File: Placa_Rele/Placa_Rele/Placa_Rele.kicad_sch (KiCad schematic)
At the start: 42 parts, among them J1 Screw_Terminal_Crusher1, J2 MixerScrewTerminal1, J3 FanScrewTerminal1, K1 FINDER-36.11, K2 FINDER-36.11, K3 FINDER-36.11, Q1 2N3904, Q2 2N3904, Q3 2N3904, U1 LM7805_TO220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

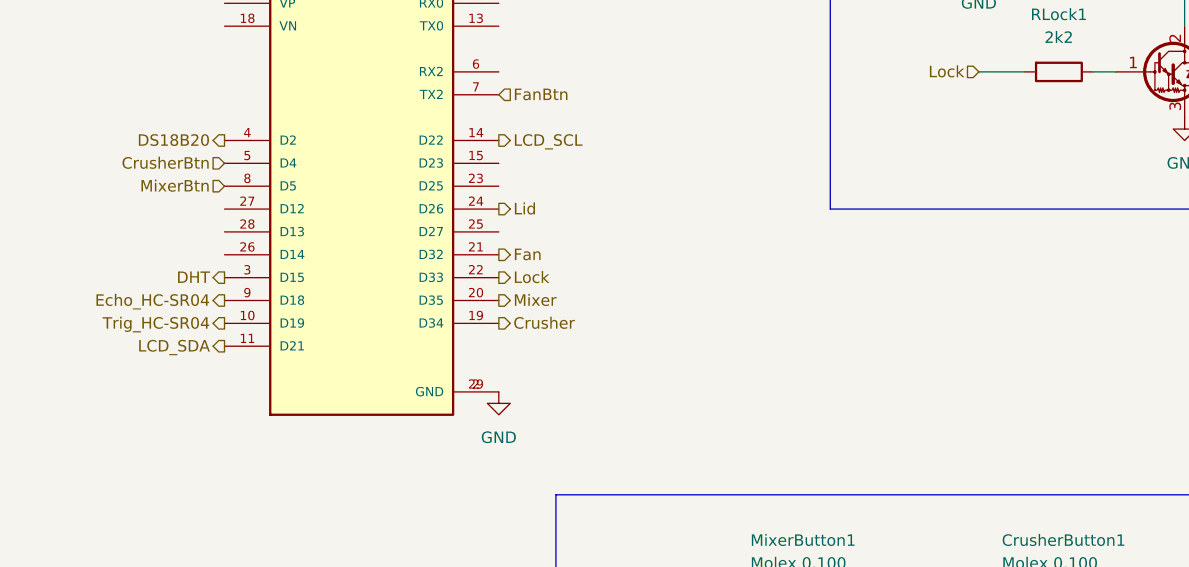
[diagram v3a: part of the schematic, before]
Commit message: feat: Agregado de placa para pcbway
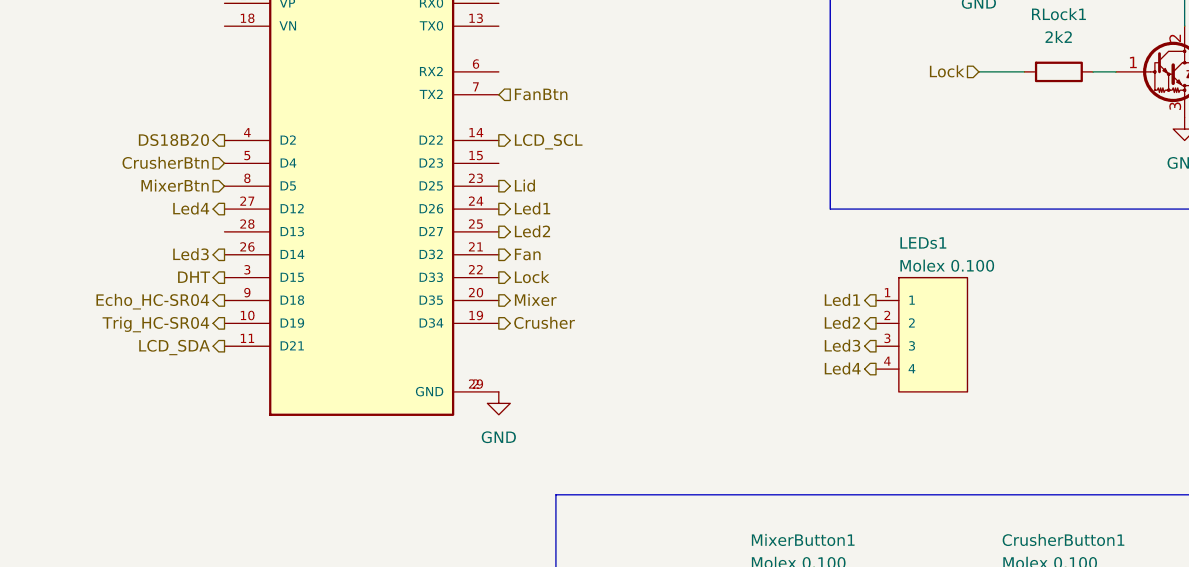
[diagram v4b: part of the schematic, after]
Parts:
- added LEDs1: Molex 0.100, Conectores_Molex:Molex_100_4pines, symbol Conectores_Molex:Molex_100_4pines
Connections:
- net Lid: now also U2.23 (D25); no longer U2.24 (D26)
- net Led2: now reaches U2.25 (D27)
- net Led2: now also LEDs1.2
- net Led3: now reaches U2.26 (D14)
- net Led3: now also LEDs1.3
- net Led4: now reaches U2.27 (D12)
- net Led4: now also LEDs1.4
- new net Led1: LEDs1.1, U2.24 (D26)
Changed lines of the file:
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@@
     (effects (font (size 1.27 1.27)) (justify left))
+  )
+  (hierarchical_label "Led1" (shape output) (at 232.41 106.68 180) (fields_autoplaced)
+    (effects (font (size 1.27 1.27)) (justify right))
   )
   (hierarchical_label "Mixer" (shape input) (at 119.38 109.22 0) (fields_autoplaced)
@@
     (effects (font (size 1.27 1.27)) (justify right))
   )
-  (hierarchical_label "Lid" (shape output) (at 190.5 96.52 0) (fields_autoplaced)
+  (hierarchical_label "Led1" (shape output) (at 190.5 96.52 0) (fields_autoplaced)
     (effects (font (size 1.27 1.27)) (justify left))
+  )
+  (hierarchical_label "Lid" (shape output) (at 190.5 93.98 0) (fields_autoplaced)
+    (effects (font (size 1.27 1.27)) (justify left))
+  )
+  (hierarchical_label "Led4" (shape output) (at 232.41 114.3 180) (fields_autoplaced)
+    (effects (font (size 1.27 1.27)) (justify right))
   )
   (hierarchical_label "Fan" (shape input) (at 119.38 152.4 0) (fields_autoplaced)
     (effects (font (size 1.27 1.27)) (justify left))
   )
+  (hierarchical_label "Led4" (shape output) (at 160.02 96.52 180) (fields_autoplaced)
+    (effects (font (size 1.27 1.27)) (justify right))
+  )
   (hierarchical_label "DHT" (shape input) (at 162.56 35.56 180) (fields_autoplaced)
     (effects (font (size 1.27 1.27)) (justify right))
@@
     (effects (font (size 1.27 1.27)) (justify right))
   )
+  (hierarchical_label "Led3" (shape output) (at 160.02 101.6 180) (fields_autoplaced)
+    (effects (font (size 1.27 1.27)) (justify right))
+  )
   (hierarchical_label "MixerBtn" (shape output) (at 208.28 144.78 180) (fields_autoplaced)
     (effects (font (size 1.27 1.27)) (justify right))
@@
     (effects (font (size 1.27 1.27)) (justify left))
   )
+  (hierarchical_label "Led3" (shape output) (at 232.41 111.76 180) (fields_autoplaced)
+    (effects (font (size 1.27 1.27)) (justify right))
+  )
   (hierarchical_label "Fan" (shape output) (at 190.5 101.6 0) (fields_autoplaced)
     (effects (font (size 1.27 1.27)) (justify left))
@@
     (effects (font (size 1.27 1.27)) (justify right))
   )
+  (hierarchical_label "Led2" (shape output) (at 232.41 109.22 180) (fields_autoplaced)
+    (effects (font (size 1.27 1.27)) (justify right))
+  )
   (hierarchical_label "3V3" (shape output) (at 190.5 66.04 0) (fields_autoplaced)
+    (effects (font (size 1.27 1.27)) (justify left))
+  )
+  (hierarchical_label "Led2" (shape output) (at 190.5 99.06 0) (fields_autoplaced)
     (effects (font (size 1.27 1.27)) (justify left))
   )
@@
         )
       )
+    )
+  )
+  (symbol (lib_id "Conectores_Molex:Molex_100_4pines") (at 237.49 109.22 0) (unit 1)
+    (in_bom yes) (on_board yes) (dnp no)
+    (property "Reference" "LEDs1" (at 234.95 100.33 0)
+      (effects (font (size 1.27 1.27)) (justify left))
+    )
+    (property "Value" "Molex 0.100" (at 234.95 102.87 0)
+      (effects (font (size 1.27 1.27)) (justify left))
+    )
+    (property "Footprint" "Conectores_Molex:Molex_100_4pines" (at 237.49 109.22 0)
+      (effects (font (size 1.27 1.27)) (justify bottom) hide)
+    )
+    (property "Datasheet" "" (at 237.49 109.22 0)
+      (effects (font (size 1.27 1.27)) hide)
+    )
+    (property "MF" "Molex" (at 237.49 109.22 0)
+      (effects (font (size 1.27 1.27)) (justify bottom) hide)
+    )
+    (property "Description" "\n4 Position Header Spacer Connector 0.100 (2.54mm) Gold, GXT™ Through Hole\n" (at 237.49 109.22 0)
+      (effects (font (size 1.27 1.27)) (justify bottom) hide)
+    )
+    (property "Package" "None" (at 237.49 109.22 0)
+      (effects (font (size 1.27 1.27)) (justify bottom) hide)
+    )
+    (property "Price" "None" (at 237.49 109.22 0)
+      (effects (font (size 1.27 1.27)) (justify bottom) hide)
+    )
+    (property "Check_prices" "https://www.snapeda.com/parts/22-11-2042/Molex/view-part/?ref=eda" (at 237.49 109.22 0)
+      (effects (font (size 1.27 1.27)) (justify bottom) hide)
+    )
+    (property "STANDARD" "Manufacturer Recommendation" (at 237.49 109.22 0)
+      (effects (font (size 1.27 1.27)) (justify bottom) hide)
+    )
+    (property "PARTREV" "BD7" (at 237.49 109.22 0)
+      (effects (font (size 1.27 1.27)) (justify bottom) hide)
+    )
+    (property "SnapEDA_Link" "https://www.snapeda.com/parts/22-11-2042/Molex/view-part/?ref=snap" (at 237.49 109.22 0)
+      (effects (font (size 1.27 1.27)) (justify bottom) hide)
+    )
+    (property "MP" "22-11-2042" (at 237.49 109.22 0)
+      (effects (font (size 1.27 1.27)) (justify bottom) hide)
+    )
+    (property "Availability" "In Stock" (at 237.49 109.22 0)
+      (effects (font (size 1.27 1.27)) (justify bottom) hide)
+    )
+    (property "MANUFACTURER" "MOLEX" (at 237.49 109.22 0)
+      (effects (font (size 1.27 1.27)) (justify bottom) hide)
+    )
+    (pin "1")
+    (pin "2")
+    (pin "3")
+    (pin "4")
+    (instances
+      (project "Placa_Rele"
+        (path "/6164fecd-2c83-41e3-903a-21871ef519e8"
+          (reference "LEDs1") (unit 1)
+        )
+      )
+      (project "AutoCompost_Placa"
+        (path "/ced4e9c8-c58e-4967-b7eb-4d589a391933"
+          (reference "LCD1") (unit 1)
+        )
+      )
